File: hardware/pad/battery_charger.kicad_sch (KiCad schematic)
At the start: 24 parts, among them J2 NTC 10k B3950, J3 Battery 2x21700 1S2P, Q1 2N7002, Q2 2N7002, Q3 FS8205A, U2 TP4056, U3 DW01A

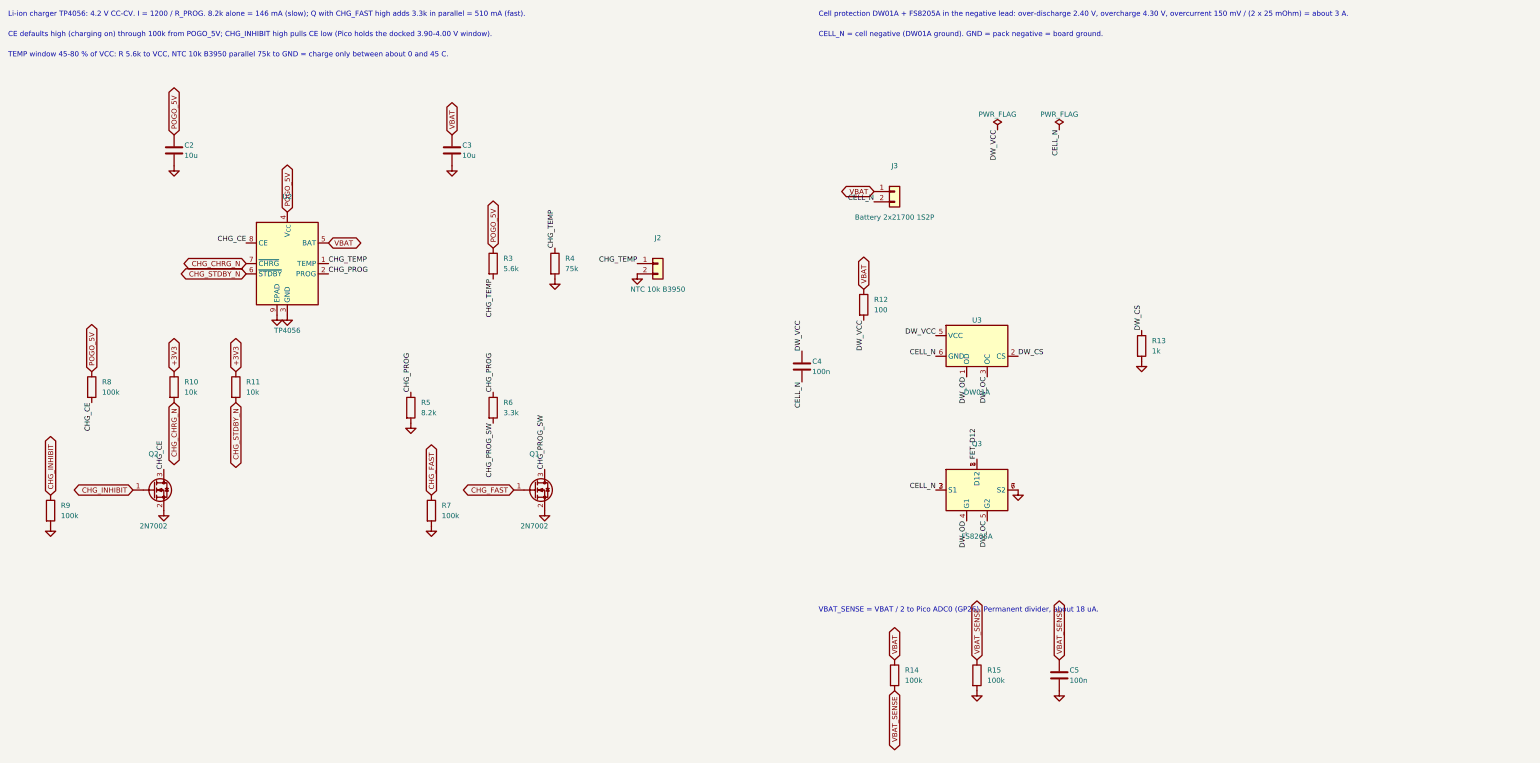
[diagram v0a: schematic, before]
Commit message: Pad schematic: hand-redrawn from the connection guide; netlist verified against the reference
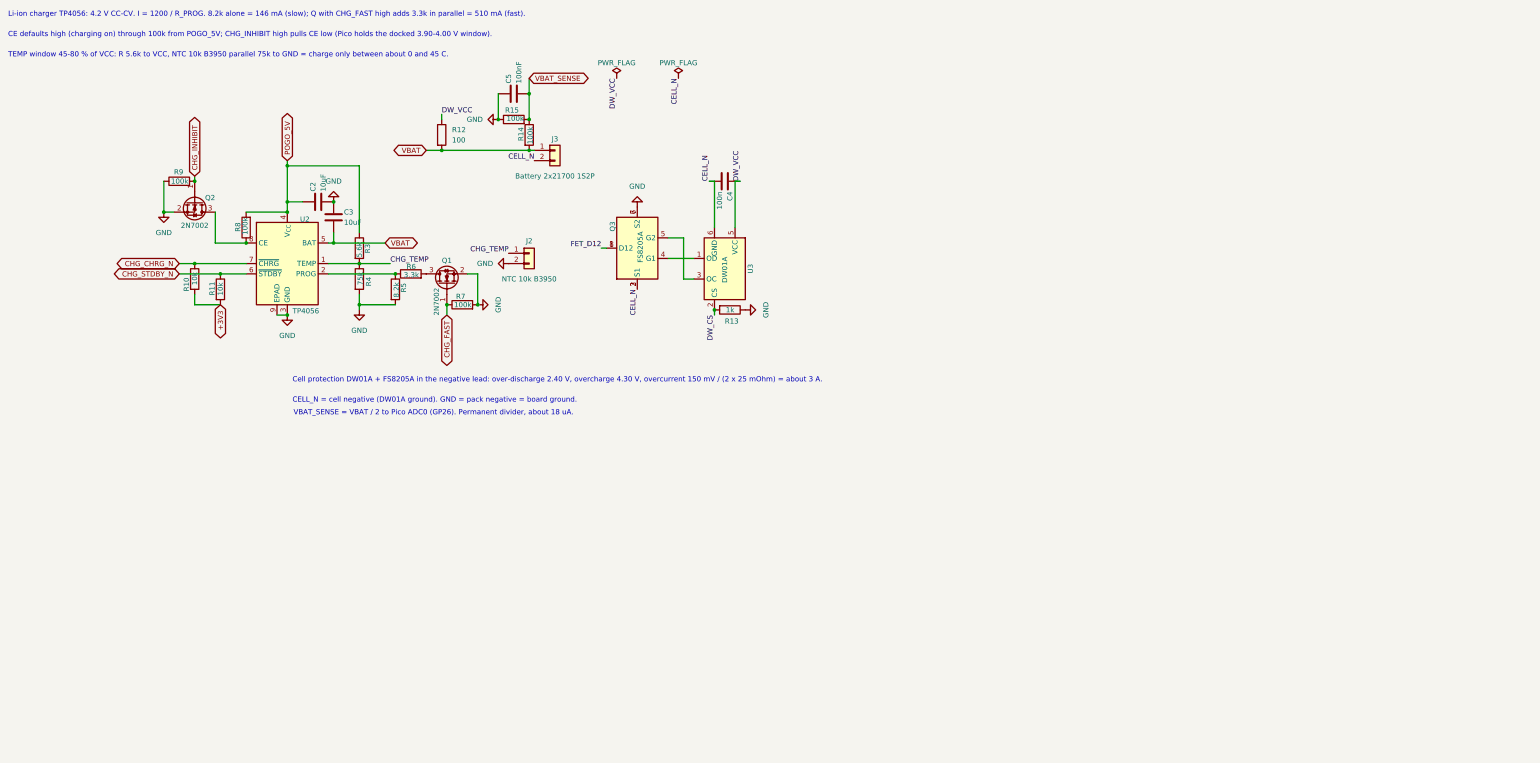
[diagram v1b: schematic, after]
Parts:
- C2, C3: value 10u -> 10uF
- C5: value 100n -> 100nF
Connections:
- net +3V3: now also R10.2, R11.2; no longer R10.1, R11.1
- net CHG_CHRG_N: now also R10.1; no longer R10.2
- net CHG_INHIBIT: now also R9.2; no longer R9.1
- net CHG_STDBY_N: now also R11.1; no longer R11.2
- net DW_CS: now also R13.2; no longer R13.1
- net DW_VCC: now also R12.1; no longer R12.2
- net GND: now also C3.1, C5.1, R13.1, R15.1, R9.1; no longer C3.2, C5.2, R13.2, R15.2, R9.2
- net POGO_5V: now also R8.2; no longer R8.1
- net VBAT: now also C3.2, R12.2, R14.2; no longer C3.1, R12.1, R14.1
- net VBAT_SENSE: now also C5.2, R14.1, R15.2; no longer C5.1, R14.2, R15.1
- net CHG_CE: no longer names the net of Q2.3 (D), U2.8 (CE)
- net CHG_CE: now also R8.1; no longer R8.2
- net CHG_PROG: no longer names the net of R5.1, R6.1, U2.2 (PROG)
- net CHG_PROG_SW: no longer names the net of Q1.3 (D), R6.2
- net DW_OC: no longer names the net of Q3.5 (G2), U3.3 (OC)
- net DW_OD: no longer names the net of Q3.4 (G1), U3.1 (OD)
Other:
- moved on the sheet: C2, J2, J3, Q3, U3
